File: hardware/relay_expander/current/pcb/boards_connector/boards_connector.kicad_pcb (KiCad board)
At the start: 2 copper layers, 38 x 31.5 mm, 3 parts, among them J2 Conn_01x20_Pin, J3 Conn_01x20_Pin

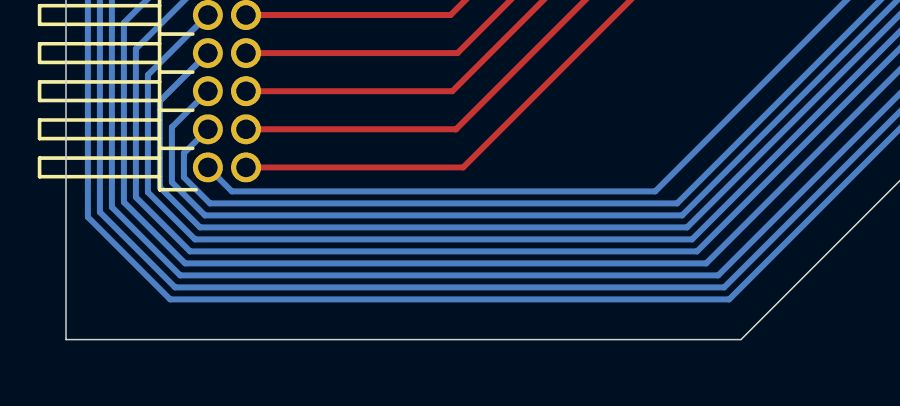
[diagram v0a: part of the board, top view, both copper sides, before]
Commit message: [FIX] add 12V trace for expanders and generate gerber for all relays related boards
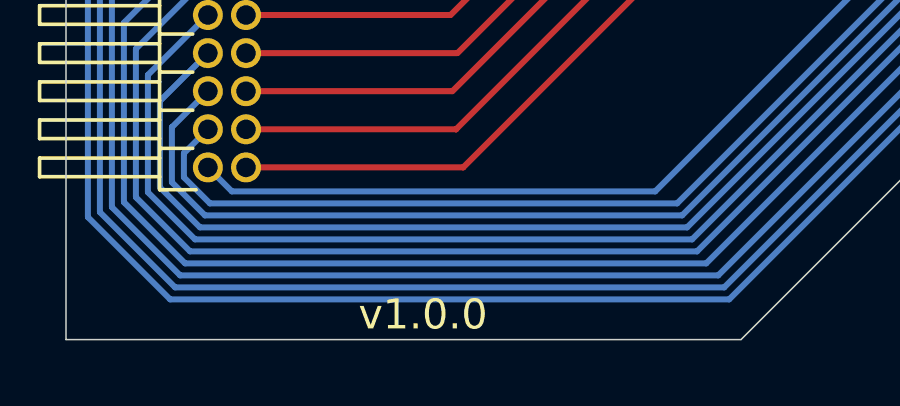
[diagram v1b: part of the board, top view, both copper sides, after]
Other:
- board text added: "v1.0.0"
